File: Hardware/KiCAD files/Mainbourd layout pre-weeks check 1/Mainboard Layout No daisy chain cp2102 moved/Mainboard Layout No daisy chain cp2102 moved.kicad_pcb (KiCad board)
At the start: 2 copper layers, 207 x 174.8 mm, 95 parts, among them J1 JST_03, J11 Conn_01x04, J12 JST_06, J13 Conn_01x08, J14 Conn_01x08, J17 PINHD_1x8_Male, J18 PINHD_1x8_Male, J19 PINHD_1x8_Male, J2 Screw_Terminal_2_P5.00mm, J20 PINHD_1x8_Male, J22 PINHD_1x8_Male, J23 PINHD_1x8_Male, J24 PINHD_1x8_Male, J25 Conn_01x04, J26 Conn_01x04, J27 Conn_01x04, J28 PINHD_1x8_Male, J3 Screw_Terminal_2_P3.50mm, J30 USB-A1VSB6, J31 JST_03, J32 USB-A1VSB6, J34 JST_03, J35 JST_03, J36 JST_03, J37 JST_03, J38 JST_03, J4 JST_06, J5 Conn_01x04, J6 JST_06, J7 JST_06, J9 Conn_01x10, Q1 BS170, Q2 2DD1664, SW1 210-4MS, SW2 210-4MS, SW3 210-4MS, SW4 210-4MS, SW8 Push_Button, SW9 Push_Button, U1 CP2102-GM, U12 ESP32-S3-WROOM-1, U2 PCA9534PW_118, U4 PCA9534PW_118

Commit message: sick weekend changes
small adjustments left our some larger protection changes till after talking to weeks
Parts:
- removed JP1, JP2: ~, PCM_SparkFun-Jumper:Jumper_2_NO
- added C17: 10uF_1210_35V, Capacitor_SMD:C_1210_3225Metric, F.Cu at (136.2, 176.1)
- added C18: 10uF_1210_35V, Capacitor_SMD:C_1210_3225Metric, F.Cu at (100.5, 78.8)
- added C19: 10uF_1210_35V, Capacitor_SMD:C_1210_3225Metric, F.Cu at (142.2, 175.8)
- added C20: 10uF_1210_35V, Capacitor_SMD:C_1210_3225Metric, F.Cu at (60.0, 185.2)
- added D1: D_Generic, Diode_THT:D_DO-201AD_P15.24mm_Horizontal, F.Cu at (156.0, 171.0)
- added R15: 0 ohmR_0805, PCM_Resistor_SMD_AKL:R_0805_2012Metric, F.Cu at (159.8, 122.3)
- added R16: 0 ohmR_0805, PCM_Resistor_SMD_AKL:R_0805_2012Metric, F.Cu at (159.8, 124.7)
- added R17: 0, Resistor_SMD:R_0805_2012Metric, F.Cu at (187.3, 31.8)
- added R18: 0, Resistor_SMD:R_0805_2012Metric, F.Cu at (189.6, 32.9)
- added TP1: TestPoint, TestPoint:TestPoint_Loop_D3.80mm_Drill2.5mm, F.Cu at (129.8, 53.7)
- added TP2: TestPoint, TestPoint:TestPoint_Loop_D3.80mm_Drill2.5mm, F.Cu at (129.5, 59.8)
- C1, C10, C11, C5: footprint PCM_SparkFun-Capacitor:Panasonic_D -> Capacitor_THT:C_Rect_L11.0mm_W3.5mm_P10.00mm_MKT
- C2: value 10uF -> 22uF
- R1, R9: value 1k -> 0
- moved J25 54.4 mm to (109.0, 176.3)
- moved J11 18.6 mm to (65.7, 183.5), turned to 90 degrees
- moved C1 1.65 mm to (64.3, 54.0), turned to 180 degrees
- moved C10 1.65 mm to (64.3, 132.4), turned to 180 degrees
- moved C11 1.65 mm to (64.3, 171.6), turned to 180 degrees
- moved C5 1.65 mm to (64.3, 93.2), turned to 180 degrees
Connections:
- C1 pad 1: +12V -> +24V
- C10 pad 1: +12V -> +24V
- C11 pad 1: +12V -> +24V
- C5 pad 1: +12V -> +24V
- J11 pad 1: +12V -> M+3.3V
- J14 pad 2: +3.3V -> /3.3V
- J17 pad 1: +12V -> +24V
- J18 pad 1: +12V -> +24V
- J19 pad 1: +12V -> +24V
- J20 pad 1: +12V -> +24V
- J30 pad SH: (no net) -> GND
- J32 pad 1: +5V_HIGHPW -> Net-(D1-K)
- R41 pad 2: +3.3V -> GND
- U12 pad 13: PI_D- -> /D-
- U12 pad 14: PI_D+ -> /D+
- U12 pad 5: unconnected-(U12-GPIO5/TOUCH5/ADC1_CH4-Pad5) -> Net-(U12-GPIO5/TOUCH5/ADC1_CH4)
- U12 pad 6: unconnected-(U12-GPIO6/TOUCH6/ADC1_CH5-Pad6) -> Net-(U12-GPIO6/TOUCH6/ADC1_CH5)
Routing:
- net +12V: track 281.3 -> 0.00 mm
- net +24V: track 237.2 -> 432.5 mm
- net GND: track 1076.7 -> 906.9 mm, vias 64 -> 220
- net +5V_HIGHPW: track 135.4 -> 38.8 mm, vias 1 -> 0
- net /D-: track 0.00 -> 75.7 mm, vias 0 -> 2
- net /D+: track 0.00 -> 72.2 mm, vias 0 -> 2
- net PI_D-: track 140.2 -> 71.1 mm
- net PI_D+: track 140.1 -> 73.4 mm
- net Net-(D1-K): track 0.00 -> 33.2 mm, vias 0 -> 1
- net Net-(U12-GPIO6/TOUCH6/ADC1_CH5): track 0.00 -> 21.7 mm, vias 0 -> 1
- net Net-(U12-GPIO5/TOUCH5/ADC1_CH4): track 0.00 -> 21.5 mm, vias 0 -> 1
- net N_ENBLE: track 124.8 -> 136.2 mm
- net nSLP: track 242.3 -> 250.2 mm
- net DIRE: track 112.1 -> 117.9 mm
- net M+3.3V: track 0.00 -> 5.82 mm
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- added copper zone on F.Cu, net +24V

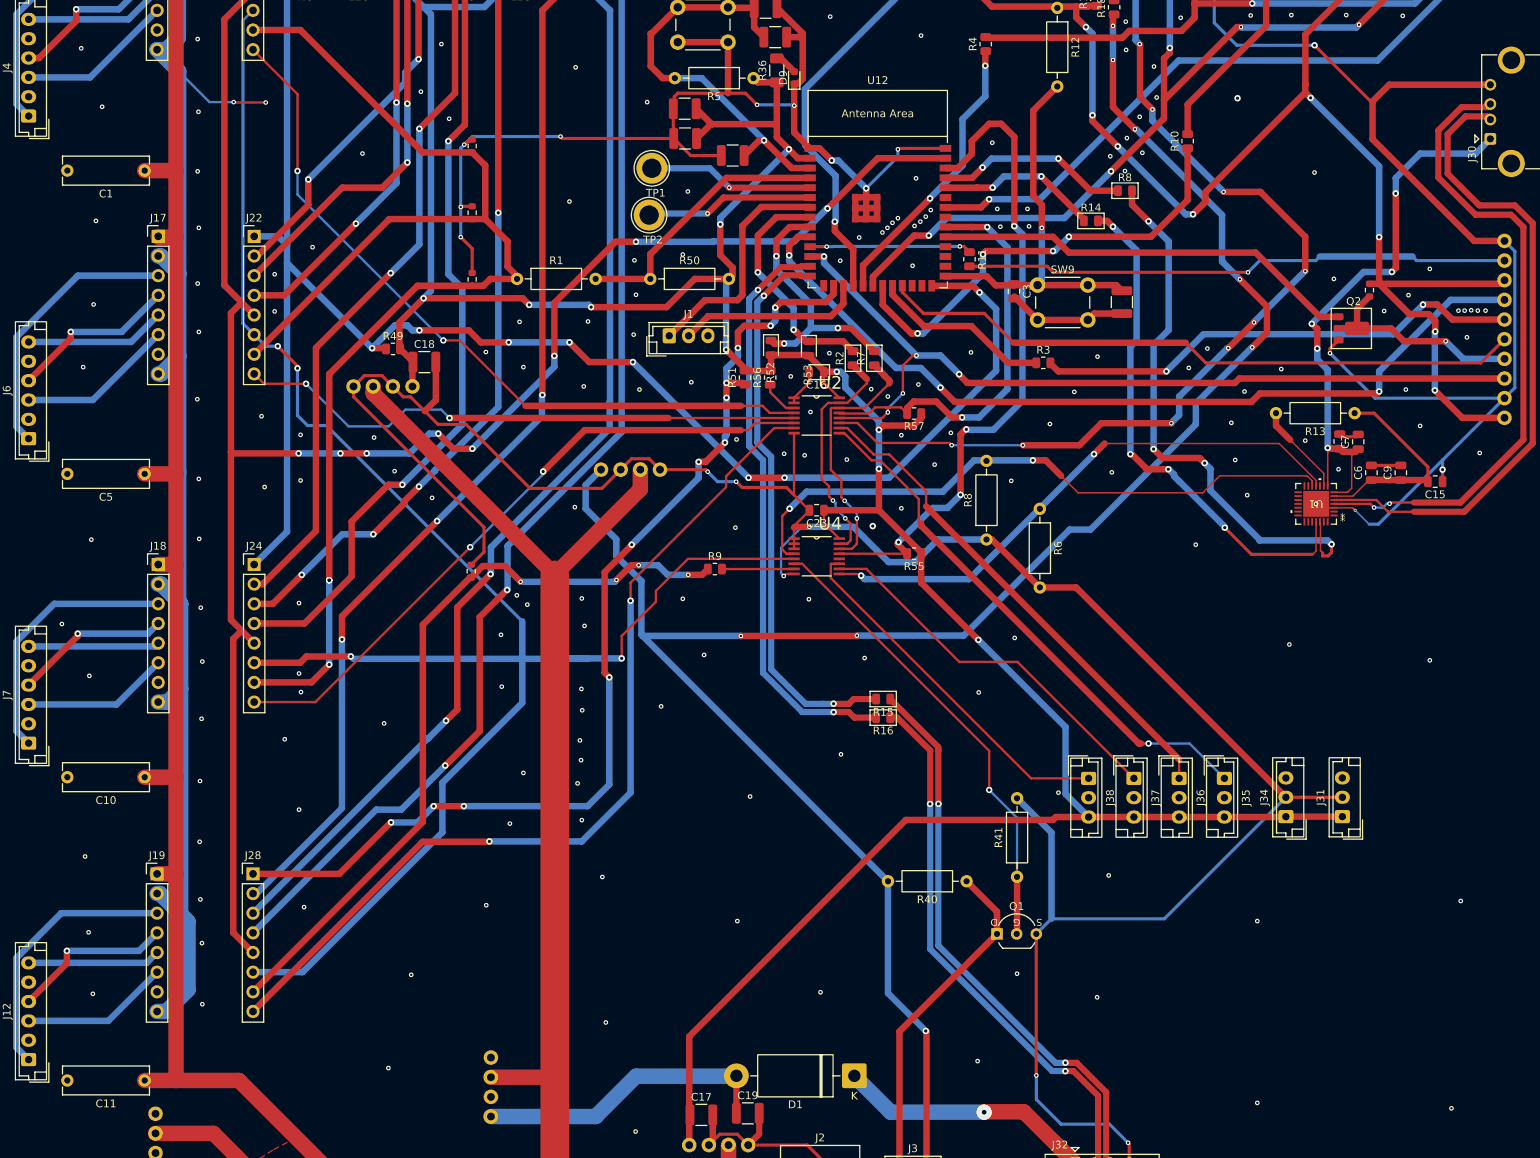
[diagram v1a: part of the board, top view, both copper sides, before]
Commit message: Compatability mods
basic modifications to work toward compatability between boards physically on the hotend
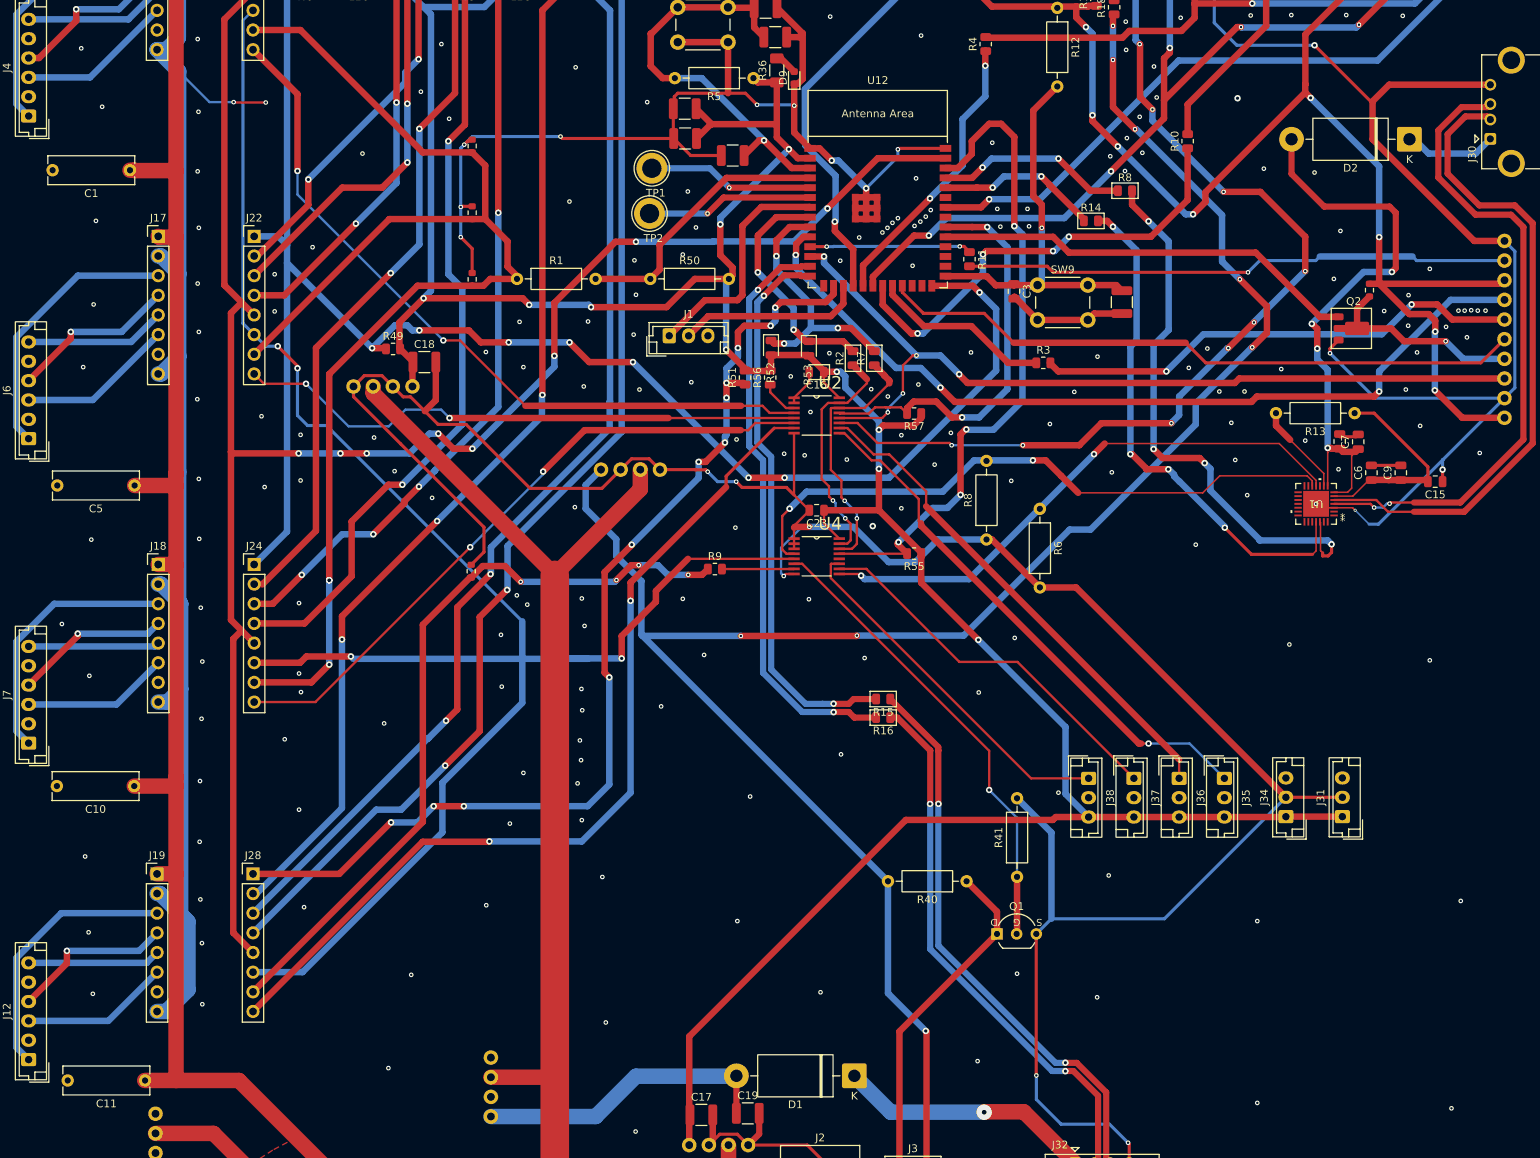
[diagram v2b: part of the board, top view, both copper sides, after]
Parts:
- added D2: D_Generic, Diode_THT:D_DO-201AD_P15.24mm_Horizontal, F.Cu at (227.8, 50.0)
- moved C5 1.98 mm to (63.0, 94.7)
- moved C1 1.90 mm to (62.4, 54.0)
- moved C10 1.77 mm to (63.0, 133.6)
- moved TP2 0.21 mm to (129.6, 59.5)
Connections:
- J30 pad 1: VBus -> Net-(D2-K)
- J30 pad SH: GND -> (no net)
- J32 pad GND: GND -> (no net)
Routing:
- net Net-(D2-K): track 0.00 -> 12.0 mm
- net +24V: track 432.5 -> 437.2 mm
- net VBus: track 73.8 -> 75.0 mm, vias 5 -> 4
- net SPI4_CLK: track 112.2 -> 111.0 mm
- net GND: vias 220 -> 227

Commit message: approved with final adjustments
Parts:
- added D3: D_Generic, Diode_THT:D_DO-201AD_P15.24mm_Horizontal, F.Cu at (157.4, 151.2)
- added D4: D_Generic, Diode_THT:D_DO-201AD_P15.24mm_Horizontal, F.Cu at (161.7, 178.7)
- J11, J25, J26, J27, J5: footprint PCM_SparkFun-Connector:1x04_P2.54mm -> PCM_SparkFun-Connector:1x03_P2.54mm
- R1: footprint Resistor_THT:R_Axial_DIN0207_L6.3mm_D2.5mm_P10.16mm_Horizontal -> Resistor_SMD:R_0805_2012Metric
- moved J25 15.9 mm to (93.2, 176.3), turned to 180 degrees
- moved J5 3.54 mm to (96.4, 84.4)
- moved R50 1.20 mm to (128.4, 68.0)
- moved R55 1.20 mm to (162.6, 103.5)
- moved C17 1.15 mm to (136.2, 174.9)
- moved J32 1.07 mm to (184.5, 181.2)
- moved R4 1.05 mm to (174.1, 37.6)
- moved J3 0.90 mm to (160.9, 184.6)
- moved R51 0.78 mm to (141.2, 80.5)
- moved R52 0.70 mm to (145.2, 77.6)
- moved J26 0.70 mm to (134.7, 179.2)
- moved C13 0.70 mm to (140.3, 51.4)
- moved J12 0.60 mm to (49.2, 168.3)
- moved J6 0.55 mm to (49.2, 88.1)
- moved J1 0.50 mm to (131.6, 75.3)
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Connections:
- J3 pad 1: SSR_Switch -> Net-(D4-K)
- J3 pad 2: +5V -> Net-(D3-K)
- R8 pad 2: TX -> RX
- U1 pad 26: TX -> RX
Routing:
- net TX: track 72.9 -> 0.00 mm, vias 4 -> 0
- net RX: track 66.8 -> 139.7 mm, vias 4 -> 8
- net GND: track 906.9 -> 860.4 mm, vias 227 -> 425
- net Net-(D3-K): track 0.00 -> 39.4 mm, vias 0 -> 1
- net SPI4_1SS: track 113.0 -> 90.3 mm, vias 5 -> 4
- net +5V: track 258.8 -> 237.8 mm, vias 8 -> 7
- net SSR_Switch: track 45.6 -> 25.7 mm
- net +5V_HIGHPW: track 38.8 -> 54.5 mm
- net STEP: track 35.0 -> 47.8 mm, vias 0 -> 2
- net Net-(D4-K): track 0.00 -> 6.21 mm
- net +3.3V: track 662.5 -> 666.0 mm
- net SPI1_1SS: track 118.7 -> 122.2 mm
- net B2_DRVE: track 34.4 -> 37.1 mm
- net Net-(U12-GPIO16/U0CTS/ADC2_CH5/XTAL_32K_N): track 33.8 -> 31.2 mm
- net +24V: track 437.2 -> 439.7 mm
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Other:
- outline, holes or cut-outs redrawn
- board text added: "VOUT"
